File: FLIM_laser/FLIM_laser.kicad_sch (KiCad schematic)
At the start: 12 parts

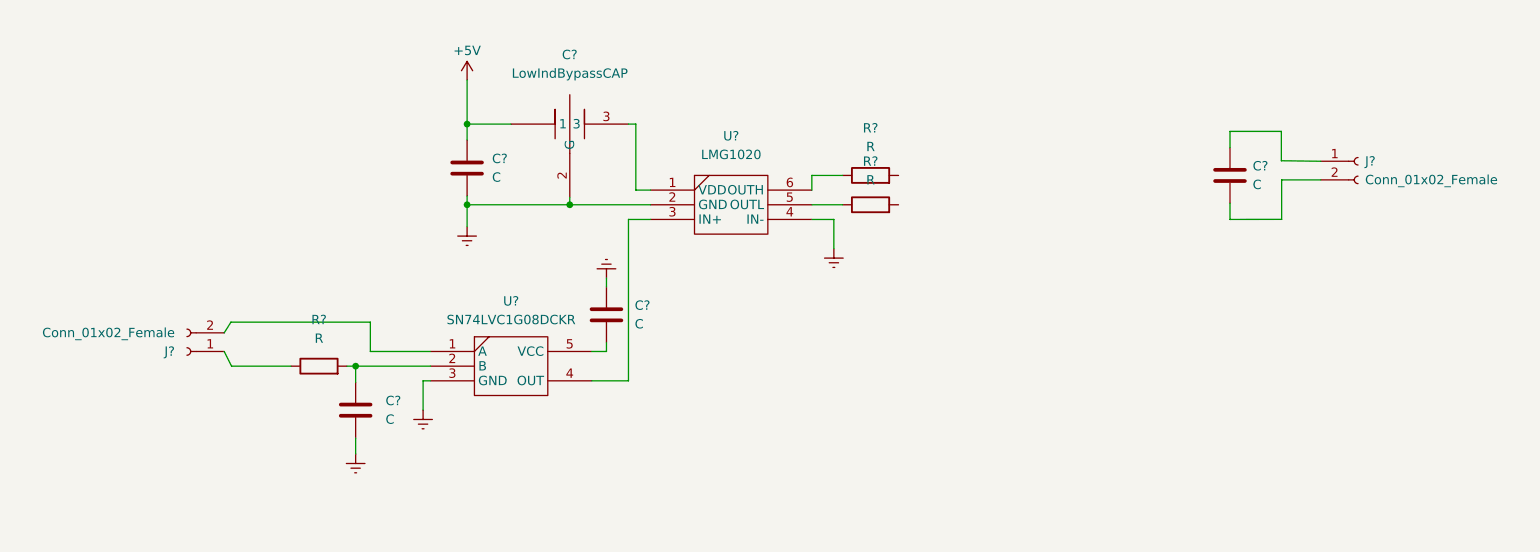
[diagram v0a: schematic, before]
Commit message: v0.2 correct connector was added
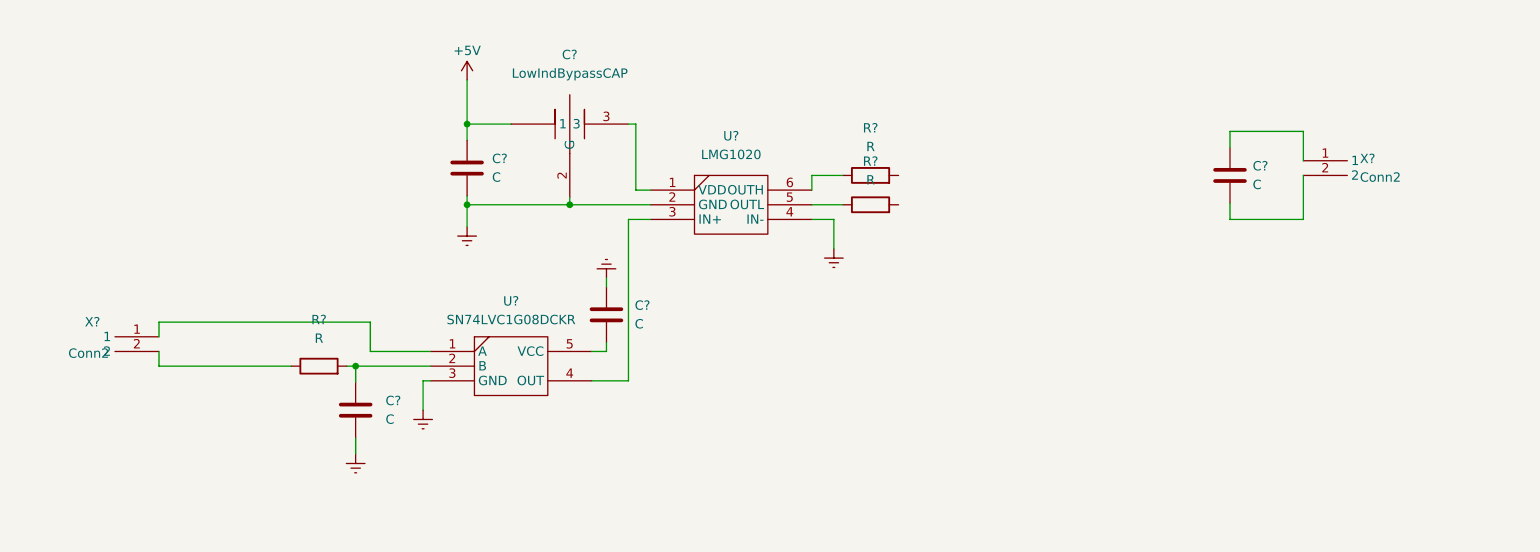
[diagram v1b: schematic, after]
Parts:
- removed J? (x2): Conn_01x02_Female, symbol Connector:Conn_01x02_Female
- added X? (x2): Conn2, symbol FLIM_LASR:Conn2
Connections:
- net at R?.1: now also X?.2
- net at U?.1 (A): now also X?.1
- net at C?.1: now also X?.1
- net at C?.2: now also X?.2
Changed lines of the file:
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@@
     (stroke (width 0) (type default) (color 0 0 0 0))
   )
-  (wire (pts (xy 202 40) (xy 209 40))
+  (wire (pts (xy 202 40) (xy 212 40))
     (stroke (width 0) (type default) (color 0 0 0 0))
   )
@@
     (stroke (width 0) (type default) (color 0 0 0 0))
   )
-  (wire (pts (xy 65.81 66) (xy 64.89 67.46))
-    (stroke (width 0) (type default) (color 0 0 0 0))
-  )
   (wire (pts (xy 92 78) (xy 92 74))
     (stroke (width 0) (type default) (color 0 0 0 0))
@@
     (stroke (width 0) (type default) (color 0 0 0 0))
   )
-  (wire (pts (xy 209 40) (xy 209 44))
-    (stroke (width 0) (type default) (color 0 0 0 0))
-  )
-  (wire (pts (xy 209.042 46.609) (xy 209.042 51.99))
-    (stroke (width 0) (type default) (color 0 0 0 0))
-  )
   (wire (pts (xy 92 74) (xy 93 74))
     (stroke (width 0) (type default) (color 0 0 0 0))
@@
     (stroke (width 0) (type default) (color 0 0 0 0))
   )
-  (wire (pts (xy 209.042 46.609) (xy 214.376 46.609))
-    (stroke (width 0) (type default) (color 0 0 0 0))
-  )
   (wire (pts (xy 98 39) (xy 104 39))
     (stroke (width 0) (type default) (color 0 0 0 0))
@@
     (stroke (width 0) (type default) (color 0 0 0 0))
   )
-  (wire (pts (xy 202 52) (xy 209.042 51.99))
-    (stroke (width 0) (type default) (color 0 0 0 0))
-  )
   (wire (pts (xy 145 48) (xy 145 46))
     (stroke (width 0) (type default) (color 0 0 0 0))
@@
     (stroke (width 0) (type default) (color 0 0 0 0))
   )
+  (wire (pts (xy 212 52) (xy 202 52))
+    (stroke (width 0) (type default) (color 0 0 0 0))
+  )
   (wire (pts (xy 117 60) (xy 117 61.19))
     (stroke (width 0) (type default) (color 0 0 0 0))
@@
     (stroke (width 0) (type default) (color 0 0 0 0))
   )
-  (wire (pts (xy 65.81 66) (xy 84.81 66))
-    (stroke (width 0) (type default) (color 0 0 0 0))
-  )
-  (wire (pts (xy 64.89 70) (xy 65.89 72))
+  (wire (pts (xy 56 66) (xy 84.81 66))
     (stroke (width 0) (type default) (color 0 0 0 0))
   )
@@
     (stroke (width 0) (type default) (color 0 0 0 0))
   )
+  (wire (pts (xy 212 44) (xy 212 40))
+    (stroke (width 0) (type default) (color 0 0 0 0))
+  )
   (wire (pts (xy 120 74) (xy 120 52))
     (stroke (width 0) (type default) (color 0 0 0 0))
@@
     (stroke (width 0) (type default) (color 0 0 0 0))
   )
-  (wire (pts (xy 209 44) (xy 214.376 44.069))
+  (wire (pts (xy 56 68) (xy 56 66))
     (stroke (width 0) (type default) (color 0 0 0 0))
   )
@@
     (stroke (width 0) (type default) (color 0 0 0 0))
   )
-  (wire (pts (xy 65.89 72) (xy 74 72))
+  (wire (pts (xy 212 46) (xy 212 52))
+    (stroke (width 0) (type default) (color 0 0 0 0))
+  )
+  (wire (pts (xy 56 72) (xy 74 72))
+    (stroke (width 0) (type default) (color 0 0 0 0))
+  )
+  (wire (pts (xy 56 70) (xy 56 72))
     (stroke (width 0) (type default) (color 0 0 0 0))
   )
@@
     (pin "1")
   )
-  (symbol (lib_id "Connector:Conn_01x02_Female") (at 59.81 70 180) (unit 1)
-    (in_bom yes) (on_board yes) (fields_autoplaced)
-    (property "Reference" "J?" (id 0) (at 58.17 70.0001 0)
-      (effects (font (size 1.27 1.27)) (justify left))
-    )
-    (property "Value" "Conn_01x02_Female" (id 1) (at 58.17 67.4601 0)
-      (effects (font (size 1.27 1.27)) (justify left))
-    )
-    (property "Footprint" "" (id 2) (at 59.81 70 0)
-      (effects (font (size 1.27 1.27)) hide)
-    )
-    (property "Datasheet" "~" (id 3) (at 59.81 70 0)
-      (effects (font (size 1.27 1.27)) hide)
-    )
-    (pin "1")
-    (pin "2")
-  )
   (symbol (lib_id "Device:C") (at 98 45 0) (unit 1)
     (in_bom yes) (on_board yes) (fields_autoplaced)
@@
     (pin "1")
   )
+  (symbol (lib_id "FLIM_LASR:Conn2") (at 218 44 0) (unit 1)
+    (in_bom yes) (on_board yes) (fields_autoplaced)
+    (property "Reference" "X?" (id 0) (at 219.71 43.7299 0)
+      (effects (font (size 1.27 1.27)) (justify left))
+    )
+    (property "Value" "Conn2" (id 1) (at 219.71 46.2699 0)
+      (effects (font (size 1.27 1.27)) (justify left))
+    )
+    (property "Footprint" "" (id 2) (at 218 44 0)
+      (effects (font (size 1.27 1.27)) hide)
+    )
+    (property "Datasheet" "" (id 3) (at 218 44 0)
+      (effects (font (size 1.27 1.27)) hide)
+    )
+    (pin "1")
+    (pin "2")
+  )
+  (symbol (lib_id "FLIM_LASR:Conn2") (at 50 68 0) (mirror y) (unit 1)
+    (in_bom yes) (on_board yes)
+    (property "Reference" "X?" (id 0) (at 48 66 0)
+      (effects (font (size 1.27 1.27)) (justify left))
+    )
+    (property "Value" "Conn2" (id 1) (at 49.23 70.2699 0)
+      (effects (font (size 1.27 1.27)) (justify left))
+    )
+    (property "Footprint" "" (id 2) (at 50 68 0)
+      (effects (font (size 1.27 1.27)) hide)
+    )
+    (property "Datasheet" "" (id 3) (at 50 68 0)
+      (effects (font (size 1.27 1.27)) hide)
+    )
+    (pin "1")
+    (pin "2")
+  )
   (symbol (lib_id "FLIM_LASR:LowIndBypassCAP") (at 112 39 0) (unit 1)
     (in_bom yes) (on_board yes) (fields_autoplaced)
@@
     )
     (property "Datasheet" "~" (id 3) (at 202 46 0)
-      (effects (font (size 1.27 1.27)) hide)
-    )
-    (pin "1")
-    (pin "2")
-  )
-  (symbol (lib_id "Connector:Conn_01x02_Female") (at 219.456 44.069 0) (unit 1)
-    (in_bom yes) (on_board yes) (fields_autoplaced)
-    (property "Reference" "J?" (id 0) (at 220.416 44.0689 0)
-      (effects (font (size 1.27 1.27)) (justify left))
-    )
-    (property "Value" "Conn_01x02_Female" (id 1) (at 220.416 46.6089 0)
-      (effects (font (size 1.27 1.27)) (justify left))
-    )
-    (property "Footprint" "" (id 2) (at 219.456 44.069 0)
-      (effects (font (size 1.27 1.27)) hide)
-    )
-    (property "Datasheet" "~" (id 3) (at 219.456 44.069 0)
       (effects (font (size 1.27 1.27)) hide)
     )
@@
       (reference "C?") (unit 1) (value "C") (footprint "")
     )
-    (path "/27adf374-12d5-4a17-990e-883a465b4fab"
-      (reference "J?") (unit 1) (value "Conn_01x02_Female") (footprint "")
-    )
-    (path "/ce71a47a-1c35-4e69-b580-d144096ab2e1"
-      (reference "J?") (unit 1) (value "Conn_01x02_Female") (footprint "")
-    )
     (path "/0dd62587-43f0-4f38-9112-5c7f17b48ba6"
       (reference "R?") (unit 1) (value "R") (footprint "")
@@
       (reference "U?") (unit 1) (value "LMG1020") (footprint "")
     )
-  )
+    (path "/49c8f6c6-7d9a-4069-b76f-713134efde3e"
+      (reference "X?") (unit 1) (value "Conn2") (footprint "")
+    )
+    (path "/4ccbd87a-6009-4c87-8808-c130f2ff1924"
+      (reference "X?") (unit 1) (value "Conn2") (footprint "")
+    )
+  )

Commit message: v0.3 circuit is ready
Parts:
- added VT?: EPC2014C, symbol FLIM_LASR:EPC2014C
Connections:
- net Earth: now also C?.2, X?.2, VT?. (Substrate)
- net at R?.2: now also R?.2, VT?. (Substrate)
- net at C?.1, X?.1: now also VT?. (Substrate)
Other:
- moved on the sheet: C?, R?, X?

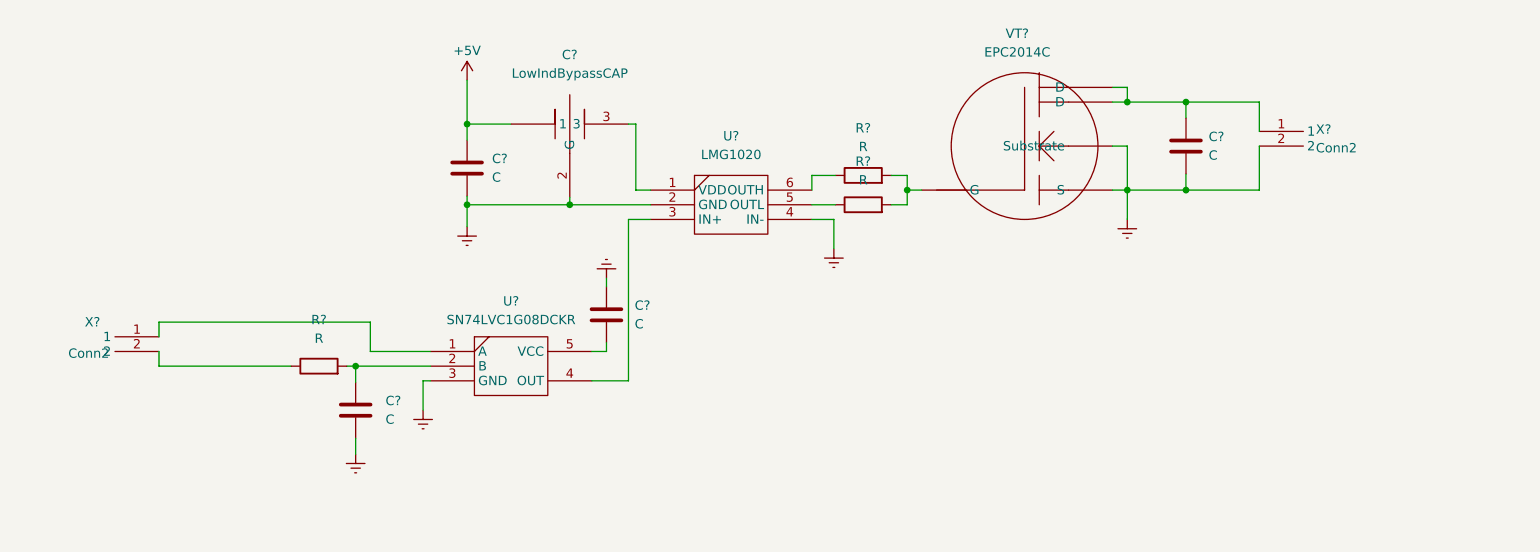
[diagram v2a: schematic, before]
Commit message: v0.4 correct symbols were added
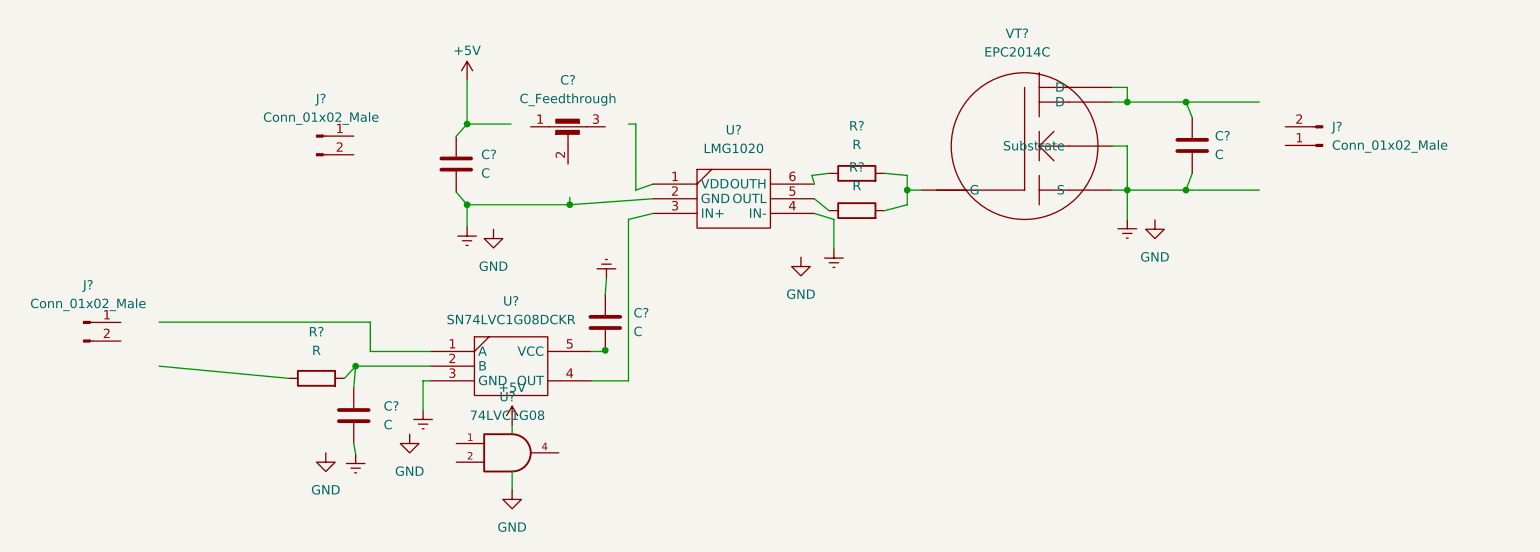
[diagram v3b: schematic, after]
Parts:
- removed C?: LowIndBypassCAP, symbol FLIM_LASR:LowIndBypassCAP
- removed X? (x2): Conn2, symbol FLIM_LASR:Conn2
- added C?: C_Feedthrough, symbol Device:C_Feedthrough
- added J? (x2): Conn_01x02_Male, Connector_PinHeader_2.54mm:PinHeader_1x02_P2.54mm_Vertical, symbol Connector:Conn_01x02_Male
- added J?: Conn_01x02_Male, Connector_PinSocket_2.54mm:PinSocket_1x02_P2.54mm_Vertical, symbol Connector:Conn_01x02_Male
- added U?: 74LVC1G08, Package_TO_SOT_SMD:SOT-353_SC-70-5_Handsoldering, symbol 74xGxx:74LVC1G08
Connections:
- net +5V: now also U?.5 (VCC)
- new net GND: U?.3 (GND)
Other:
- moved on the sheet: C?, R?, U?

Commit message: v0.5 power source was added
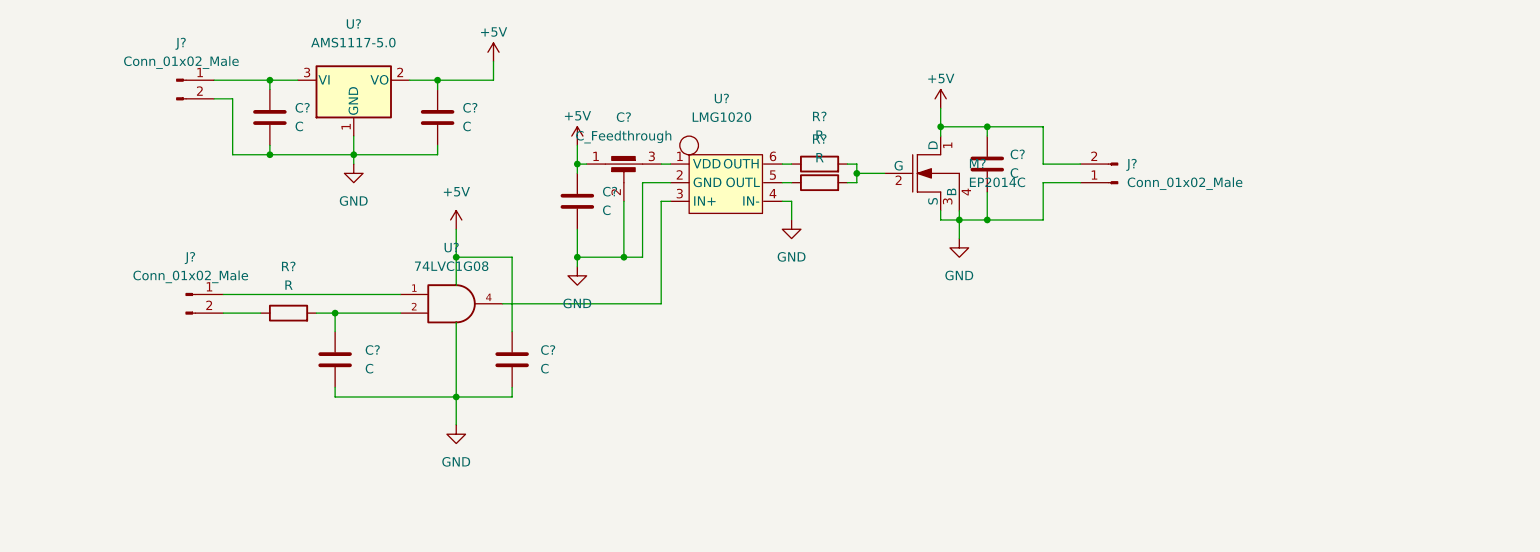
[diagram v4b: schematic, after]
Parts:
- removed J?: Conn_01x02_Male, Connector_PinHeader_2.54mm:PinHeader_1x02_P2.54mm_Vertical, symbol Connector:Conn_01x02_Male
- removed U?: SN74LVC1G08DCKR, symbol FLIM_LASR:SN74LVC1G08DCKR
- removed U?: LMG1020, symbol FLIM_LASR:LMG1020
- removed VT?: EPC2014C, symbol FLIM_LASR:EPC2014C
- added C? (x2): C, symbol Device:C
- added J?: Conn_01x02_Male, Connector_PinHeader_2.54mm:PinHeader_1x02_P2.54mm_Vertical, symbol Connector:Conn_01x02_Male
- added M?: EP2014C, Package_TO_SOT_SMD:SOT-23-6_Handsoldering, symbol pspice:MNMOS
- added U?: AMS1117-5.0, Package_TO_SOT_SMD:SOT-223-3_TabPin2, symbol Regulator_Linear:AMS1117-5.0
- added U?: LMG1020, symbol FLIM_LASR:LMG1020
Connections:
- net +5V: now also C?.1, C?.1, C?.1, J?.2 (Pin_2), C?.1, M?.1 (D), U?.2 (VO)
- net GND: now also C?.2, C?.2, C?.2, C?.2, C?.2, J?.1 (Pin_1), C?.2, C?.2, J?.2 (Pin_2), M?.3 (S), M?.4 (B), U?.1 (GND), U?.2 (GND), U?.4 (IN-)
- net at R?.1: now also J?.2 (Pin_2)
- net at C?.1, R?.2: now also U?.2
- net at R?.2, R?.2: now also M?.2 (G)
- net at R?.1: now also U?.5 (OUTL)
- net at J?.1 (Pin_1): now also U?.1
- net at C?.3: now also U?.1 (VDD)
- net at U?.4: now also U?.3 (IN+)
- net at R?.1: now also U?.6 (OUTH)
- removed net Earth: C?.1, C?.2, C?.2, C?.2
- new net: C?.1, J?.1 (Pin_1), U?.3 (VI)
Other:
- moved on the sheet: C?, J?, R?, U?

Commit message: v0.6 input shottky was added
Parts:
- added D?: PMEG40T10ER, Diode_SMD:Nexperia_CFP3_SOD-123W, symbol Diode:PMEG40T10ER
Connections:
- net at C?.1, U?.3 (VI): now also D?.1 (K); no longer J?.1 (Pin_1)
- new net: D?.2 (A), J?.1 (Pin_1)
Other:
- moved on the sheet: J?
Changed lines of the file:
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@@
   (junction (at 113.03 57.15) (diameter 0) (color 0 0 0 0)
   )
+  (junction (at 71.12 33.02) (diameter 0) (color 0 0 0 0)
+  )
   (junction (at 96.52 76.2) (diameter 0) (color 0 0 0 0)
   )
@@
   (junction (at 162.56 39.37) (diameter 0) (color 0 0 0 0)
   )
-  (junction (at 71.12 33.02) (diameter 0) (color 0 0 0 0)
-  )
   (wire (pts (xy 113.03 57.15) (xy 113.03 58.42))
     (stroke (width 0) (type default) (color 0 0 0 0))
@@
     (stroke (width 0) (type default) (color 0 0 0 0))
   )
-  (wire (pts (xy 66.04 35.56) (xy 63.5 35.56))
+  (wire (pts (xy 66.04 35.56) (xy 58.42 35.56))
     (stroke (width 0) (type default) (color 0 0 0 0))
   )
@@
     (stroke (width 0) (type default) (color 0 0 0 0))
   )
+  (wire (pts (xy 58.42 33.02) (xy 60.96 33.02))
+    (stroke (width 0) (type default) (color 0 0 0 0))
+  )
   (wire (pts (xy 80.01 64.77) (xy 80.01 67.31))
     (stroke (width 0) (type default) (color 0 0 0 0))
@@
     (stroke (width 0) (type default) (color 0 0 0 0))
   )
-  (wire (pts (xy 63.5 33.02) (xy 71.12 33.02))
-    (stroke (width 0) (type default) (color 0 0 0 0))
-  )
   (wire (pts (xy 121.92 57.15) (xy 119.38 57.15))
     (stroke (width 0) (type default) (color 0 0 0 0))
@@
   )
   (wire (pts (xy 104.14 57.15) (xy 96.52 57.15))
+    (stroke (width 0) (type default) (color 0 0 0 0))
+  )
+  (wire (pts (xy 68.58 33.02) (xy 71.12 33.02))
     (stroke (width 0) (type default) (color 0 0 0 0))
   )
@@
     (pin "1")
   )
-  (symbol (lib_id "Connector:Conn_01x02_Male") (at 58.42 33.02 0) (unit 1)
-    (in_bom yes) (on_board yes) (fields_autoplaced)
-    (property "Reference" "J?" (id 0) (at 59.055 27.94 0))
-    (property "Value" "Conn_01x02_Male" (id 1) (at 59.055 30.48 0))
-    (property "Footprint" "Connector_PinHeader_2.54mm:PinHeader_1x02_P2.54mm_Vertical" (id 2) (at 58.42 33.02 0)
-      (effects (font (size 1.27 1.27)) hide)
-    )
-    (property "Datasheet" "~" (id 3) (at 58.42 33.02 0)
+  (symbol (lib_id "Connector:Conn_01x02_Male") (at 53.34 33.02 0) (unit 1)
+    (in_bom yes) (on_board yes) (fields_autoplaced)
+    (property "Reference" "J?" (id 0) (at 53.975 27.94 0))
+    (property "Value" "Conn_01x02_Male" (id 1) (at 53.975 30.48 0))
+    (property "Footprint" "Connector_PinHeader_2.54mm:PinHeader_1x02_P2.54mm_Vertical" (id 2) (at 53.34 33.02 0)
+      (effects (font (size 1.27 1.27)) hide)
+    )
+    (property "Datasheet" "~" (id 3) (at 53.34 33.02 0)
       (effects (font (size 1.27 1.27)) hide)
     )
@@
     )
     (property "Datasheet" "~" (id 3) (at 73.66 64.77 0)
+      (effects (font (size 1.27 1.27)) hide)
+    )
+    (pin "1")
+    (pin "2")
+  )
+  (symbol (lib_id "Diode:PMEG40T10ER") (at 64.77 33.02 180) (unit 1)
+    (in_bom yes) (on_board yes) (fields_autoplaced)
+    (property "Reference" "D?" (id 0) (at 65.0875 26.67 0))
+    (property "Value" "PMEG40T10ER" (id 1) (at 65.0875 29.21 0))
+    (property "Footprint" "Diode_SMD:Nexperia_CFP3_SOD-123W" (id 2) (at 64.77 28.575 0)
+      (effects (font (size 1.27 1.27)) hide)
+    )
+    (property "Datasheet" "https://assets.nexperia.com/documents/data-sheet/PMEG40T10ER.pdf" (id 3) (at 64.77 33.02 0)
       (effects (font (size 1.27 1.27)) hide)
     )
@@
       (reference "C?") (unit 1) (value "C") (footprint "")
     )
+    (path "/1d0c62cc-4a41-44a3-88fd-2959325bf540"
+      (reference "D?") (unit 1) (value "PMEG40T10ER") (footprint "Diode_SMD:Nexperia_CFP3_SOD-123W")
+    )
     (path "/0d8f75cd-0b83-4543-ae7c-d647edde10e6"

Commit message: v0.7 PCB prototype was created, components were decomposed
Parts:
- removed U?: LMG1020, symbol FLIM_LASR:LMG1020
- added U2: LMG1020, FLIM_laser:BGA-6_2x3_0.8x1.2mm, symbol FLIM_LASR:LMG1020
- C1, C2, C3, C5, C6, C7: renamed from C?; footprint (none) -> Capacitor_SMD:C_0603_1608Metric_Pad1.08x0.95mm_HandSolder
- C4: renamed from C?; footprint (none) -> FLIM_laser:YFF18PW0J474M
- M1: renamed from M?; footprint Package_TO_SOT_SMD:SOT-23-6_Handsoldering -> FLIM_laser:EPC2014C
- R1, R2, R3: renamed from R?; footprint (none) -> Resistor_SMD:R_0603_1608Metric_Pad0.98x0.95mm_HandSolder
- gave numbers to parts that had none: 6
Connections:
- net +5V: now also J2.1 (Pin_1); no longer J2.2 (Pin_2)
- net GND: now also J2.2 (Pin_2), U2.B1 (GND), U2.C2 (IN-); no longer J2.1 (Pin_1)
- net at R2.1: now also U2.B2 (OUTL)
- net at C4.3: now also U2.A1 (VDD)
- net at U3.4: now also U2.C1 (IN+)
- net at R1.1: now also U2.A2 (OUTH)
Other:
- moved on the sheet: J2
